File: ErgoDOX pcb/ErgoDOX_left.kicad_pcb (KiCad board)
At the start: 2 copper layers, 182.8 x 158.9 mm, 97 parts, among them J1 AudioJack4, J2 USB_B_Micro, SW0:10 SW0:3, SW0:11 SW0:2, SW0:12 SW0:1, SW0:7 SW0:6, SW0:8 SW0:5, SW0:9 SW0:4, SW1 TS-1187A-B-A-B, SW1:10 SW1:3, SW1:11 SW1:2, SW1:12 SW1:1, SW1:13 SW1:0, SW1:9 SW1:4, SW2:10 SW2:3, SW2:11 SW2:2, SW2:12 SW2:1, SW2:13 SW2:0, SW2:7 SW2:6, SW2:8 SW2:5, SW2:9 SW2:4, SW3:10 SW3:3, SW3:11 SW3:2, SW3:12 SW3:1, SW3:13 SW3:0, SW3:8 SW3:5, SW3:9 SW3:4, SW4:10 SW4:3, SW4:11 SW4:2, SW4:12 SW4:1, SW4:13 SW4:0, SW4:7 SW4:6, SW4:8 SW4:5, SW4:9 SW4:4, SW5:10 SW5:3, SW5:11 SW5:2, SW5:12 SW5:1, SW5:13 SW5:0, SW5:7 SW5:6, SW5:8 SW5:5, SW5:9 SW5:4, U1 ATmega32U4-MU, U2 MCP23018

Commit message: finished LH routing
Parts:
- removed R6, R7: 1k, Resistors_SMD:R_0603
- removed U2: MCP23018, Housings_SSOP:SSOP-24_5.3x8.2mm_Pitch0.65mm
- added C1: 10p, Capacitors_SMD:C_0603, F.Cu at (52.3, 40.7)
- added C2: 10p, Capacitors_SMD:C_0603, F.Cu at (58.8, 40.5)
- added C3: 1u, Capacitors_SMD:C_0603, F.Cu at (50.0, 33.2)
- added C4: 1u, Capacitors_SMD:C_0603, F.Cu at (58.8, 26.7)
- added C5: 100n, Capacitors_SMD:C_0603, F.Cu at (63.0, 37.0)
- added C6: 100n, Capacitors_SMD:C_0603, F.Cu at (50.5, 30.2)
- added R5: 1k, Resistors_SMD:R_0603, F.Cu at (72.7, 31.2)
- added Y1: 16MHz, Crystals:Crystal_SMD_3225-4pin_3.2x2.5mm, F.Cu at (55.7, 40.6)
- SW0:10, SW0:11, SW0:12, SW0:7, SW0:8, SW0:9, SW2:10, SW2:11, SW2:12, SW2:13, SW2:7, SW2:8, SW2:9, SW3:10, SW3:11, SW3:12, SW3:13, SW3:8, SW3:9, SW4:10, SW4:11, SW4:12, SW4:13, SW4:7, SW4:8, SW4:9, SW5:10, SW5:11, SW5:12, SW5:13, SW5:7, SW5:8, SW5:9, SX1:7, SX1:8: moved to F.Cu
- moved R9 233.8 mm to (62.8, 35.0), turned to 180 degrees
- moved R10 232.3 mm to (62.8, 33.0), turned to 180 degrees
- moved SW1 221.6 mm to (36.3, 38.5)
- moved U1 219.2 mm to (56.1, 33.6)
- moved D2:13 213.4 mm to (40.3, 120.5), turned to 180 degrees
- moved R8 194.1 mm to (61.5, 28.5), turned to 90 degrees
- moved D2:12 189.4 mm to (62.3, 121.5)
- moved J2 181.5 mm to (90.3, 23.5), turned to 180 degrees
- moved R1 163.8 mm to (89.3, 29.0), turned to 90 degrees
- moved R2 163.1 mm to (91.0, 29.0), turned to 90 degrees
- moved SW0:7 158.6 mm to (192.9, 130.8), turned to 155 degrees
- moved SW2:13 155.9 mm to (36.1, 111.7), turned to 180 degrees
- moved SW3:13 155.9 mm to (36.1, 92.6), turned to 180 degrees
- moved SW4:13 155.9 mm to (36.1, 73.6), turned to 180 degrees
- moved SW5:13 155.9 mm to (36.1, 54.5), turned to 180 degrees
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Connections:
- LED_C1 pad 2: (no net) -> Net-(LED_C1-Pad2)
- U1 pad 12: (no net) -> /LED_C
- U1 pad 16: (no net) -> Net-(C1-Pad2)
- U1 pad 17: (no net) -> Net-(C2-Pad1)
- U1 pad 6: (no net) -> Net-(C3-Pad1)
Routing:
- net /COL6: track 0.00 -> 253.4 mm, vias 0 -> 2
- net /COL4: track 0.00 -> 244.7 mm, vias 0 -> 2
- net /COL5: track 0.00 -> 220.6 mm, vias 0 -> 2
- net /ROW2: track 46.0 -> 253.3 mm
- net /COL10: track 0.00 -> 191.7 mm, vias 0 -> 2
- net Net-(D2:7-Pad2): track 173.2 -> 7.71 mm, vias 1 -> 0
- net /COL1: track 0.00 -> 160.5 mm
- net /COL11: track 0.00 -> 159.9 mm, vias 0 -> 2
- net VCC: track 0.00 -> 146.0 mm, vias 0 -> 6
- net /COL0: track 0.00 -> 124.6 mm, vias 0 -> 6
- net /ROW1: track 156.2 -> 275.4 mm
- net /ROW3: track 91.5 -> 201.6 mm
- net /SDA: track 0.00 -> 87.4 mm, vias 0 -> 2
- net /ROW4: track 121.7 -> 207.4 mm
- net /ROW0: track 269.4 -> 351.6 mm, vias 1 -> 0
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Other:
- outline, holes or cut-outs redrawn
- board text added: "Dox"
- board text added: "Ergo"
- board text removed: "LEFT HAND"
- board text removed: "ProfetKeyboards.com"
- board text removed: "RIGHT HAND"

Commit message: USB breakout draft
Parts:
- added J101: USB_C_Receptacle_USB2.0, Connectors_USB:USB_C_Receptacle_Amphenol_12401610E4-2A, F.Cu at (180.3, 92.8)
- added J102: USB_B_Mini, ErgoDOX:CUI_UJ2-MABH-1-SMT, F.Cu at (180.3, 56.3)
- added J2: USB_B, ErgoDOX:usb_breakout, F.Cu at (91.4, 29.5)
- added J201: USB_B, ErgoDOX:usb_breakout, F.Cu at (181.3, 98.8)
- added J202: USB_B, ErgoDOX:usb_breakout, F.Cu at (181.3, 61.3)
- added J203: USB_B, ErgoDOX:usb_breakout, F.Cu at (181.3, 80.0)
- moved J103 102.6 mm to (180.0, 73.2)
- moved R1 2.06 mm to (88.8, 27.0), turned to 0 degrees
- moved R2 1.25 mm to (89.8, 29.0), turned to 0 degrees
- renumbered J2 to J103
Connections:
- J103 pad 1: VCC -> Net-(J103-Pad1)
- J103 pad 2: /USB- -> Net-(J103-Pad2)
- J103 pad 3: /USB+ -> Net-(J103-Pad3)
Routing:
- net Net-(J101-PadA4): track 0.00 -> 18.1 mm
- net Net-(J102-Pad1): track 0.00 -> 13.8 mm
- net Net-(J103-Pad1): track 0.00 -> 11.9 mm
- net Net-(J101-PadA7): track 0.00 -> 8.55 mm, vias 0 -> 2
- net Net-(J103-Pad3): track 0.00 -> 8.01 mm
- net Net-(J103-Pad2): track 0.00 -> 7.75 mm
- net Net-(J101-PadA6): track 0.00 -> 6.15 mm
- net /D-: track 55.3 -> 49.2 mm
- net Net-(J102-Pad3): track 0.00 -> 5.63 mm
- net /D+: track 55.9 -> 50.6 mm
- net Net-(J102-Pad2): track 0.00 -> 5.09 mm
- net VCC: track 146.0 -> 151.1 mm, vias 6 -> 7
- net /USB+: track 3.26 -> 5.47 mm
- net /SDA: track 87.4 -> 88.3 mm
- net GND: track 9.84 -> 9.91 mm, vias 78 -> 104
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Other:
- outline, holes or cut-outs redrawn
- board text removed: "Dox"
- board text removed: "Ergo"

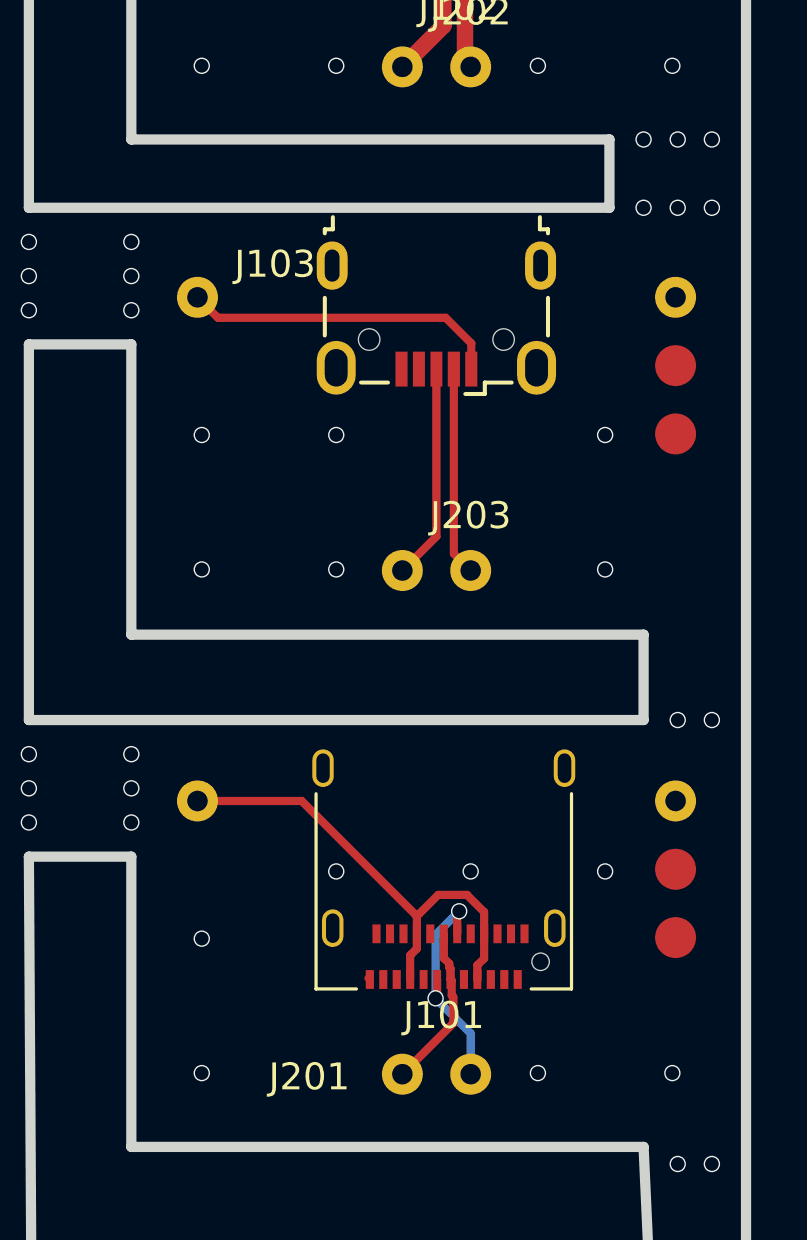
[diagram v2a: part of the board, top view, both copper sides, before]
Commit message: Updated USB footprints
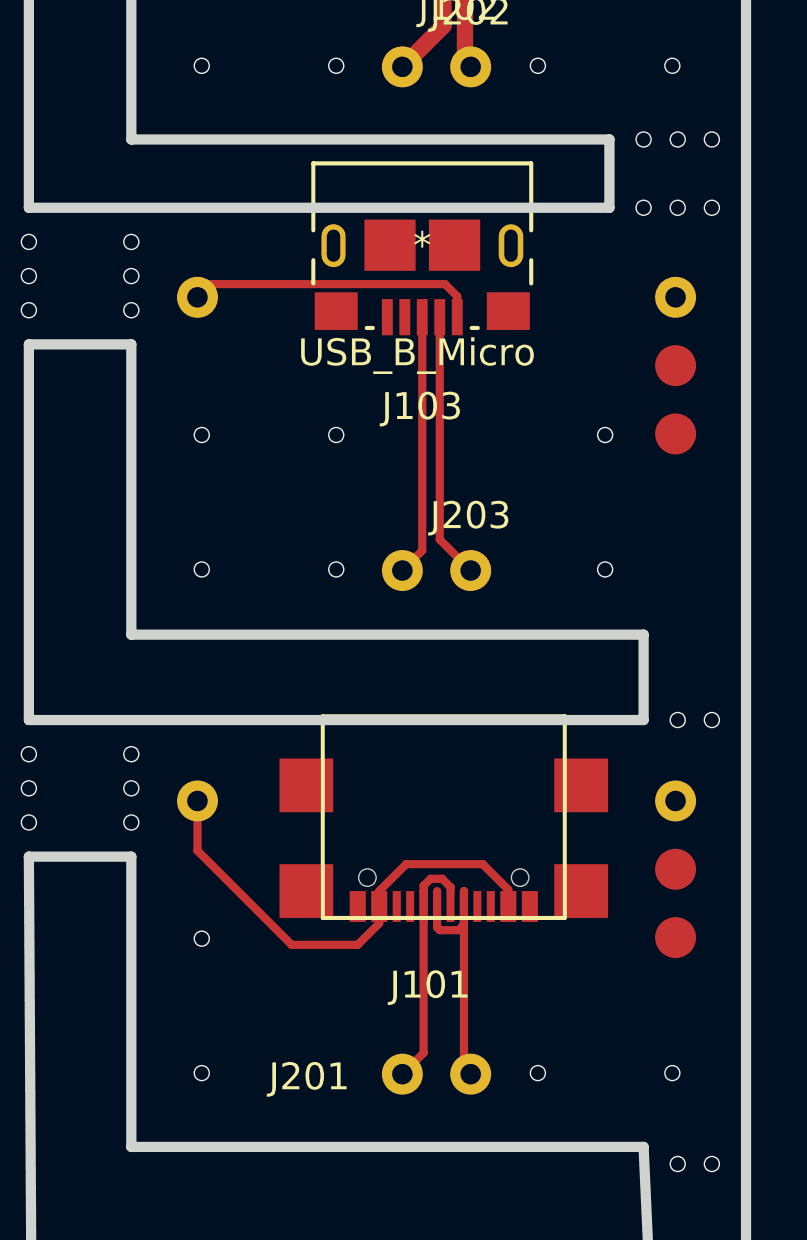
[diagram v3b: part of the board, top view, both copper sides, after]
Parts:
- J101: footprint Connectors_USB:USB_C_Receptacle_Amphenol_12401610E4-2A -> ErgoDOX:USB4110-GF-A
- J103: footprint Connectors_USB:USB_Micro-B_Wuerth-629105150521 -> ErgoDOX:10118193-0001LF
- moved J103 2.74 mm to (179.5, 70.5)
- moved J101 1.73 mm to (180.3, 94.5)
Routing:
- net Net-(J101-PadA6): track 6.15 -> 8.72 mm
- net Net-(J103-Pad2): track 7.75 -> 9.90 mm
- net Net-(J101-PadA7): track 8.55 -> 10.6 mm, vias 2 -> 0
- net Net-(J103-Pad3): track 8.01 -> 9.73 mm
- net Net-(J101-PadA4): track 18.1 -> 17.2 mm
- net Net-(J103-Pad1): track 11.9 -> 11.3 mm
- net (no net): vias 20 -> 17

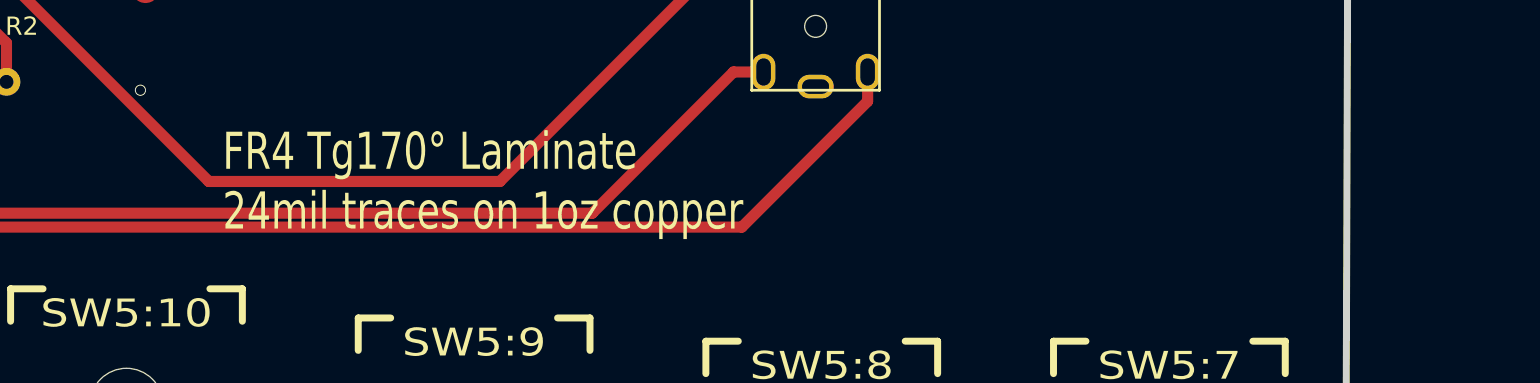
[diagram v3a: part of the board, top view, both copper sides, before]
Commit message: Added revision, generated gerbers
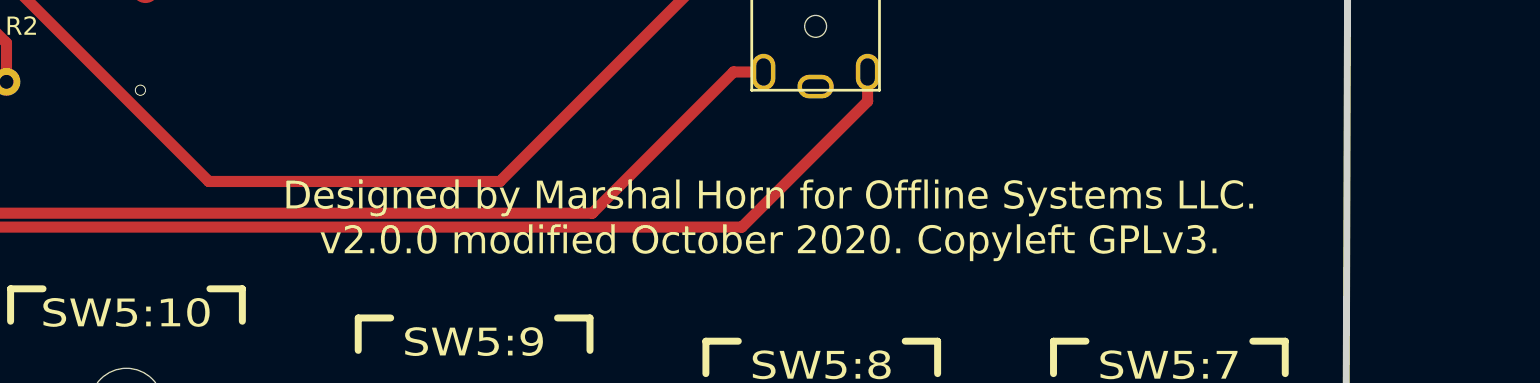
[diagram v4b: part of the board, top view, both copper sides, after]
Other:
- board text added: "Designed by Marshal Horn for Offline Systems LLC. v2.0.0 modified October 2020. Copyleft GPLv3."
- board text removed: "FR4 Tg170° Laminate 24mil traces on 1oz copper"

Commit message: Removed soldermask clearance
Re-generated gerbers for left PCB
Added BOM and placement file for left PCB
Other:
- rule pad_to_mask_clearance: 0.0508 -> 0
